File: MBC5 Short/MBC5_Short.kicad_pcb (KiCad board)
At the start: 2 copper layers, 51 x 30.7 mm, 1 part, among them J1 GameBoy_GamePak_AGB-002

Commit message: Initialize PCB configuration (blank template)
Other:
- outline, holes or cut-outs redrawn
- net class Default removed

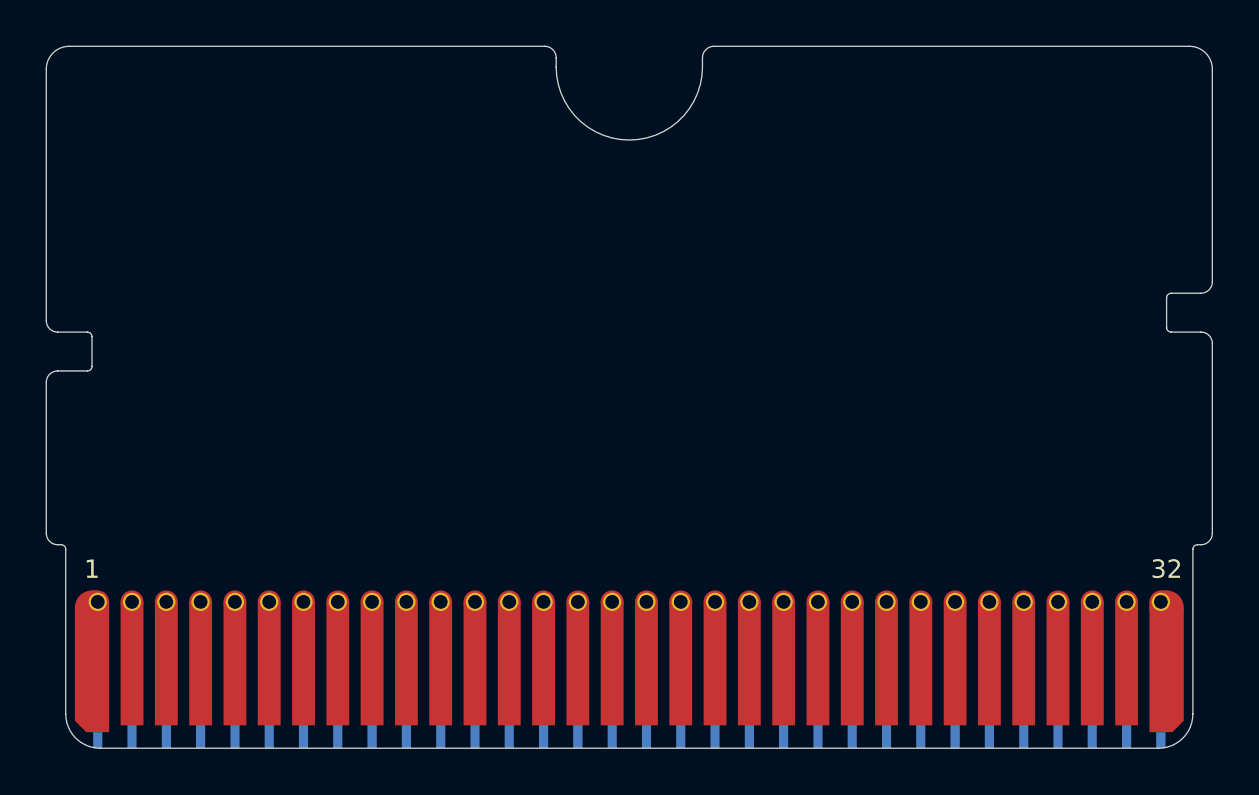
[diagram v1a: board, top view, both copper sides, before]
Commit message: Update GameBoy_GamePak_AGB-002 template with pads instead of just shapes
This also copies over all the nets I was using for the pins
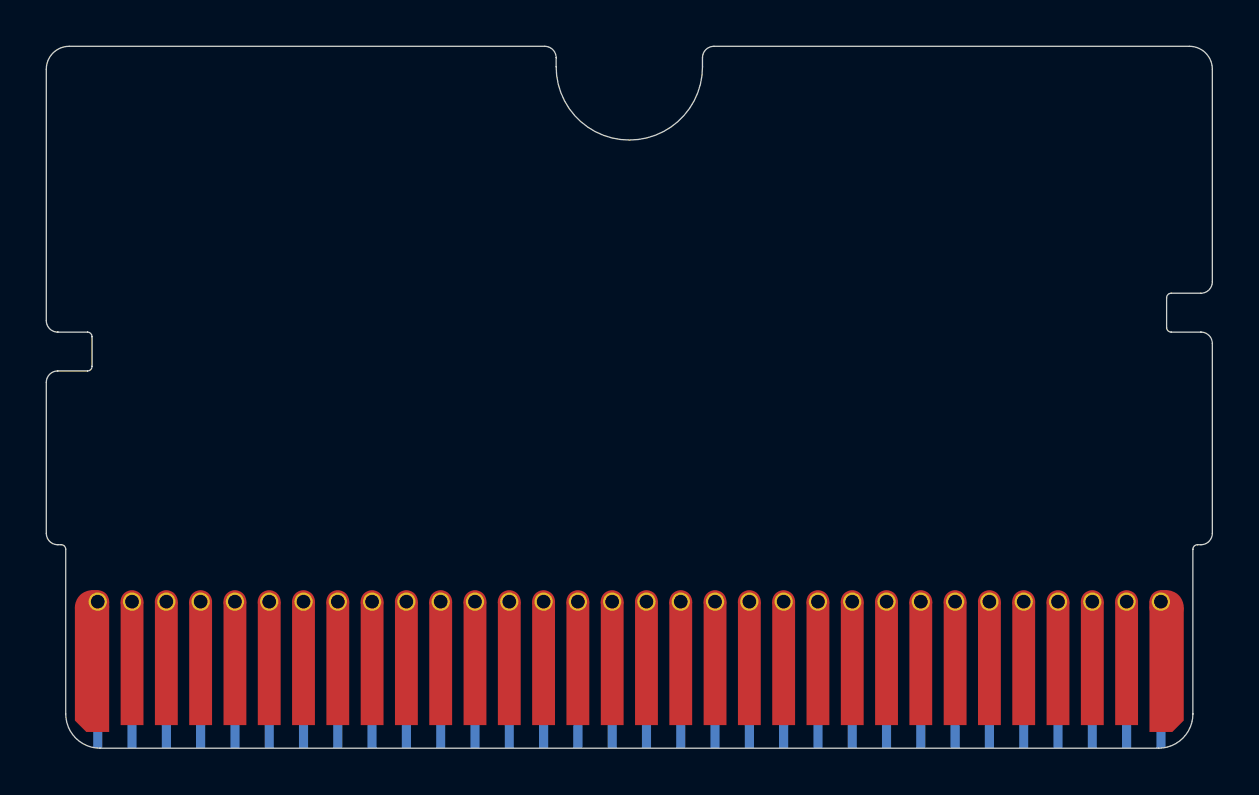
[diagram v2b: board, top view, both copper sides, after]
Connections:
- net Net-(J1-Pad1) renamed +5V
- net Net-(J1-Pad10) renamed A4
- net Net-(J1-Pad11) renamed A5
- net Net-(J1-Pad12) renamed A6
- net Net-(J1-Pad13) renamed A7
- net Net-(J1-Pad14) renamed A8
- net Net-(J1-Pad15) renamed A9
- net Net-(J1-Pad16) renamed A10
- net Net-(J1-Pad17) renamed A11
- net Net-(J1-Pad18) renamed A12
- net Net-(J1-Pad19) renamed A13
- net Net-(J1-Pad20) renamed A14
- net Net-(J1-Pad21) renamed A15
- net Net-(J1-Pad22) renamed D0
- net Net-(J1-Pad23) renamed D1
- net Net-(J1-Pad24) renamed D2
- net Net-(J1-Pad25) renamed D3
- net Net-(J1-Pad26) renamed D4
- net Net-(J1-Pad27) renamed D5
- net Net-(J1-Pad28) renamed D6
- net Net-(J1-Pad29) renamed D7
- net Net-(J1-Pad3) renamed WR
- net Net-(J1-Pad30) renamed RESET
- net Net-(J1-Pad31) renamed WE_SND
- net Net-(J1-Pad32) renamed GND
- net Net-(J1-Pad4) renamed RD
- net Net-(J1-Pad5) renamed CS
- net Net-(J1-Pad6) renamed A0
- net Net-(J1-Pad7) renamed A1
- net Net-(J1-Pad8) renamed A2
- net Net-(J1-Pad9) renamed A3
- J1 pad 2: Net-(J1-Pad2) -> (no net)
